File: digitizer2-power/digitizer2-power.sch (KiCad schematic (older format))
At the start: 37 parts, among them P1 CONN_01X02, P2 CONN_01X05, Q1 Q_NPN_BEC, Q2 Q_NPN_BEC, U1 LM3674, U2 LM3671MF-1.8, U3 LM3671MF-1.5, U4 LM3671MF-3.3

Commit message: Build new digitizer2-power board from buck module
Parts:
- removed C15, C16, C17: 4.7uF, Capacitors_SMD:C_0805, symbol C_Small
- removed D1: LED, LEDs:LED_0805, symbol LED
- removed P1: CONN_01X02, Pin_Headers:Pin_Header_Straight_1x02, symbol CONN_01X02
- removed P2: CONN_01X05, Pin_Headers:Pin_Header_Straight_1x05, symbol CONN_01X05
- removed Q1, Q2: Q_NPN_BEC, TO_SOT_Packages_SMD:SOT-23, symbol Q_NPN_BEC
- removed U1: LM3674, TO_SOT_Packages_SMD:SOT-23-5, symbol LM3674
- removed U2: LM3671MF-1.8, TO_SOT_Packages_SMD:SOT-23-5, symbol LM3671
- removed U3: LM3671MF-1.5, TO_SOT_Packages_SMD:SOT-23-5, symbol LM3671
- removed U4: LM3671MF-3.3, TO_SOT_Packages_SMD:SOT-23-5, symbol LM3671
- added D1, D2, D3, D4: D_Schottky_Small, Diodes_SMD:SMA_Standard, symbol D_Schottky_Small
- added D5, D6, D7, D8: D_Schottky_Small, Diodes_SMD:SOD-123, symbol D_Schottky_Small
- added D9: 1.8V, LEDs:LED_0603, symbol Led_Small
- added L5: 2.2uH, digitizer2_modules:IHLP-1212BZ-11, symbol L_Small
- added P1: CONN_01X04, Pin_Headers:Pin_Header_Straight_1x04, symbol CONN_01X04
- added P2: CONN_02X04, Pin_Headers:Pin_Header_Straight_2x04, symbol CONN_02X04
- added R10, R12: Ren2, Resistors_SMD:R_0603_HandSoldering, symbol R_Small
- added R11, R9: Ren1, Resistors_SMD:R_0603_HandSoldering, symbol R_Small
- added R13: 750, Resistors_SMD:R_0603_HandSoldering, symbol R_Small
- added R8: div2, Resistors_SMD:R_0603_HandSoldering, symbol R_Small
- added U1, U2, U3, U4: ADP2301, TO_SOT_Packages_SMD:SOT-23-6, symbol ADP2301
- C1, C4, C6: value 4.7uF -> 10uF; footprint Capacitors_SMD:C_0805 -> Capacitors_SMD:C_1206; MPN (none) -> GRM32DR61C106KA01L
- C10, C11, C12, C3: value 4.7uF -> C_Small; footprint Capacitors_SMD:C_0805 -> Capacitors_SMD:C_1210; MPN (none) -> GRM32ER61A476KE20L
- C13, C14: value 4.7uF -> C_Small; footprint Capacitors_SMD:C_0805 -> Capacitors_SMD:c_elec_5x5.7
- C2, C7, C8, C9: value 4.7uF -> 0.1uF; footprint Capacitors_SMD:C_0805 -> Capacitors_SMD:C_0603_HandSoldering
- C5: value 18pF -> 10uF; footprint Capacitors_SMD:C_0603 -> Capacitors_SMD:C_1206; MPN (none) -> GRM32DR61C106KA01L
- L1, L2, L3, L4: MPN (none) -> IHLP1212BZER2R2M11
- R1: value 200k -> div1; footprint Resistors_SMD:R_0805 -> Resistors_SMD:R_0603_HandSoldering
- R2: value 200k -> div2; footprint Resistors_SMD:R_0805 -> Resistors_SMD:R_0603_HandSoldering
- R3: value 10k -> div1; footprint Resistors_SMD:R_0805 -> Resistors_SMD:R_0603_HandSoldering
- R4: value 10k -> div2; footprint Resistors_SMD:R_0805 -> Resistors_SMD:R_0603_HandSoldering
- R5: value 1k -> div1; footprint Resistors_SMD:R_0805 -> Resistors_SMD:R_0603_HandSoldering
- R6: value 1k -> div2; footprint Resistors_SMD:R_0805 -> Resistors_SMD:R_0603_HandSoldering
- R7: value 600 -> div1; footprint Resistors_SMD:R_0805 -> Resistors_SMD:R_0603_HandSoldering
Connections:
- net labels added: 5V0_IN, BST1, BST2, BST3, BST4, EN1V8, FB1, FB2, FB3, FB4, PGOOD1V8, SW1, SW2, SW3, SW4
- net labels removed: 1V0_ENABLED
- wire segments 74 -> 77
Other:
- note added: "TODO: Ven > 4V"
- note removed: "1.0V configuration"
- note removed: "VCC_AUX"
- note removed: "VCC_CCO_DRAM"
- note removed: "VCC_CCO_USB, VCC_FTDI"
- note removed: "VCC_INT, VCC_BRAM"

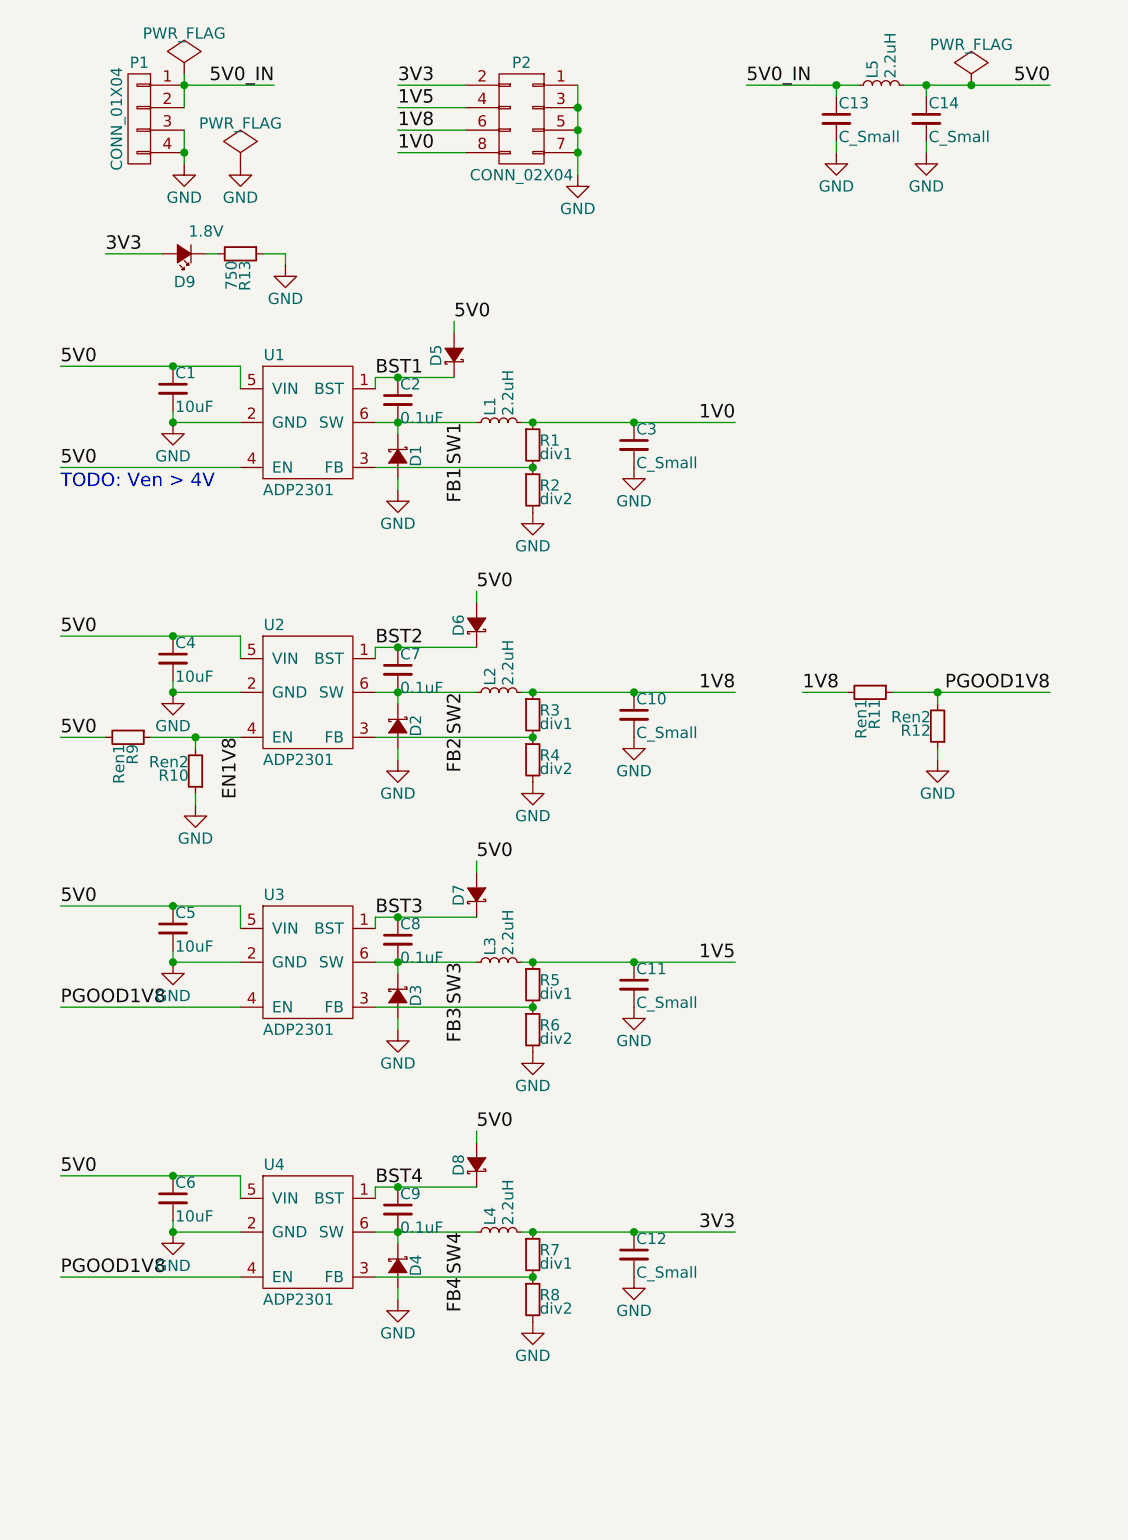
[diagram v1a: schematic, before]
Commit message: Fill in last details for power supply, cleanup
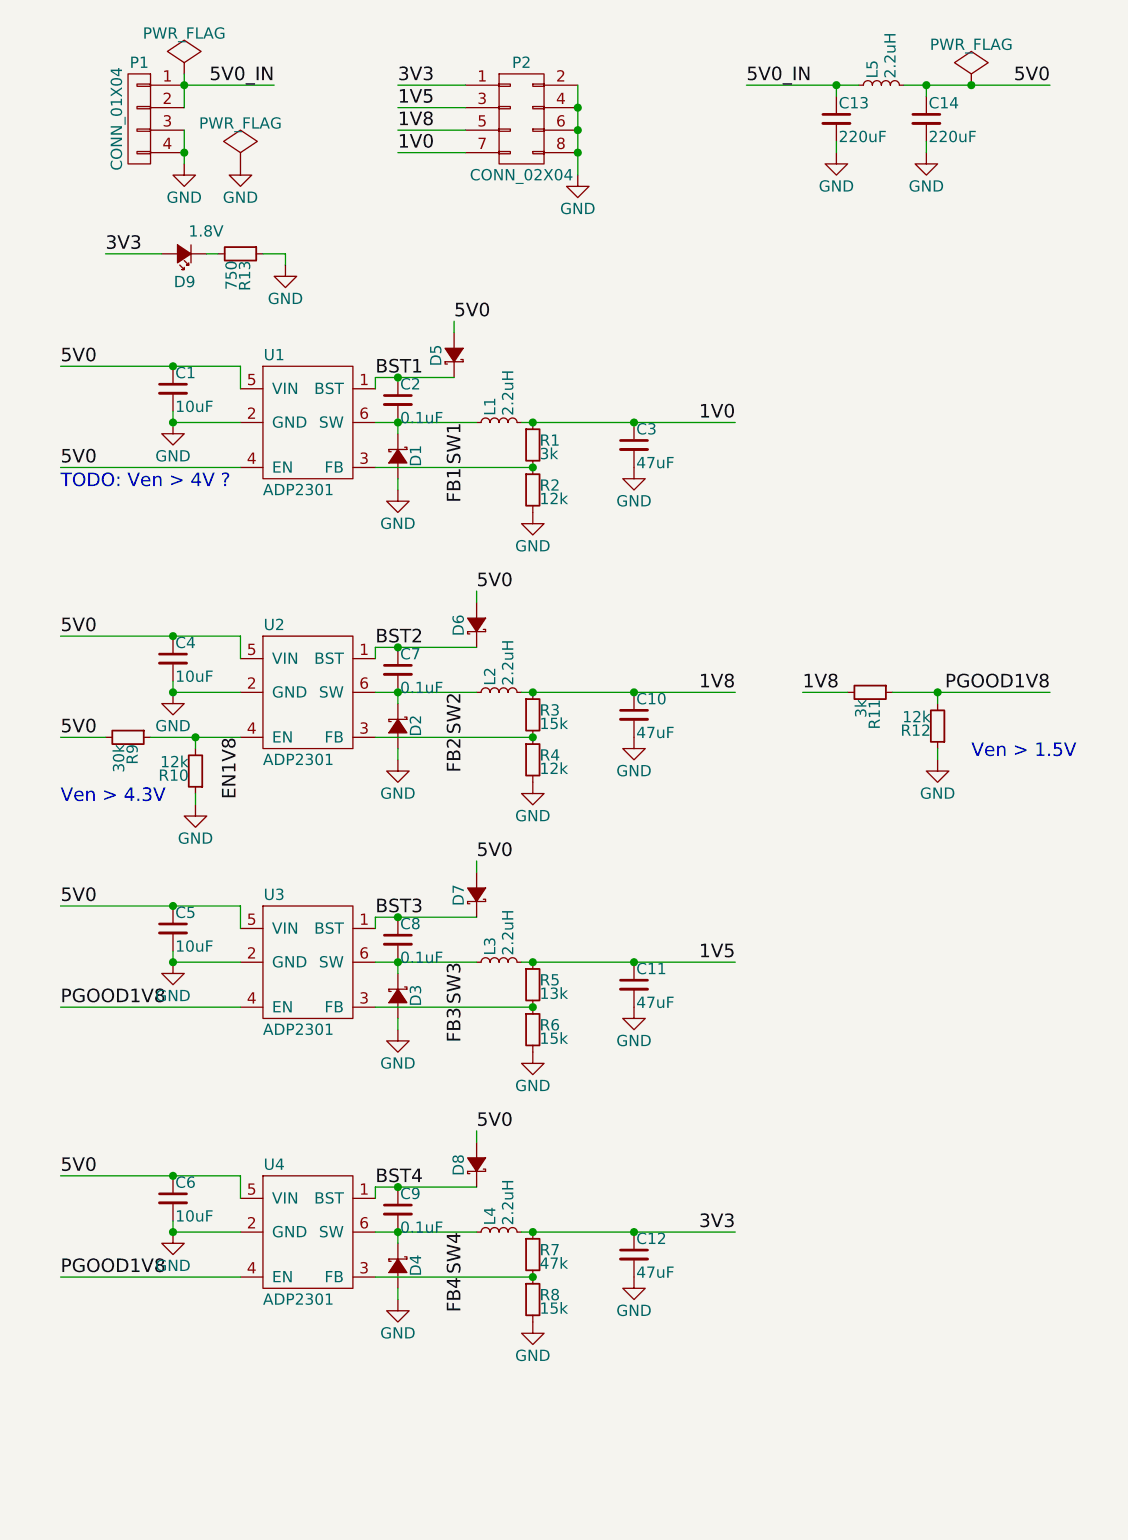
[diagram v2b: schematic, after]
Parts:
- C10, C11, C12, C3: value C_Small -> 47uF
- C13, C14: value C_Small -> 220uF; MPN (none) -> 6SVPE220MW
- C2, C7, C8, C9: MPN (none) -> GRM188R72A104KA35D
- R1: value div1 -> 3k
- R10, R12: value Ren2 -> 12k
- R11: value Ren1 -> 3k
- R2, R4: value div2 -> 12k
- R3: value div1 -> 15k
- R5: value div1 -> 13k
- R6, R8: value div2 -> 15k
- R7: value div1 -> 47k
- R9: value Ren1 -> 30k
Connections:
- net 1V0: now also P2.7 (P7); no longer P2.8 (P8)
- net 1V5: now also P2.3 (P3); no longer P2.4 (P4)
- net 1V8: now also P2.5 (P5); no longer P2.6 (P6)
- net 3V3: now also P2.1 (P1); no longer P2.2 (P2)
- net GND: now also P2.2 (P2), P2.4 (P4), P2.6 (P6), P2.8 (P8); no longer P2.1 (P1), P2.3 (P3), P2.5 (P5), P2.7 (P7)
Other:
- note added: "TODO: Ven > 4V ?"
- note added: "Ven > 1.5V"
- note added: "Ven > 4.3V"
- note removed: "TODO: Ven > 4V"
